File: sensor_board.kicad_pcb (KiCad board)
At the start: 2 copper layers, 28 parts, among them J1 DB9, P1 CONN_2, P2 CONN_2, P3 TORCH_ON, P4 ARC_OK, P5 TEST_POINTS, Q1 MOSFET_N, Q2 RELAY

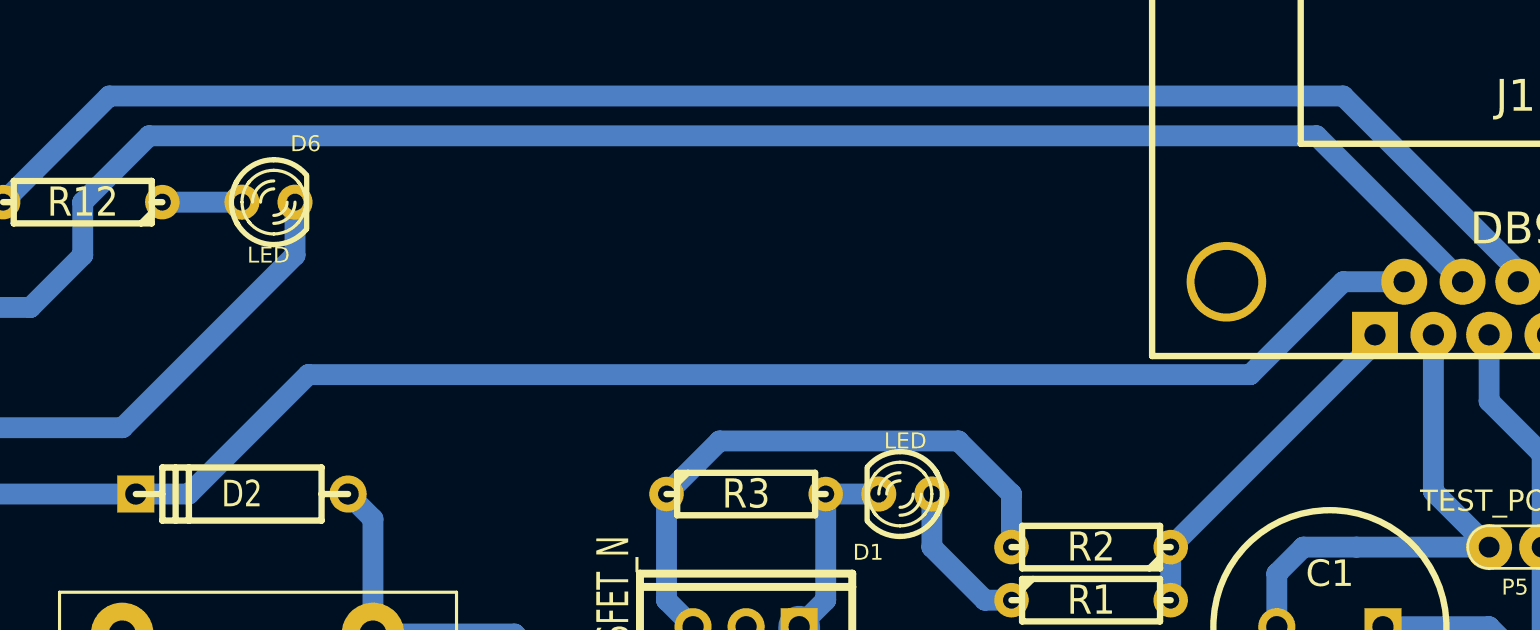
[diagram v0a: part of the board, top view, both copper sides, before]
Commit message: Fixed sensor board schematics- it's not wise to power relay from regulator
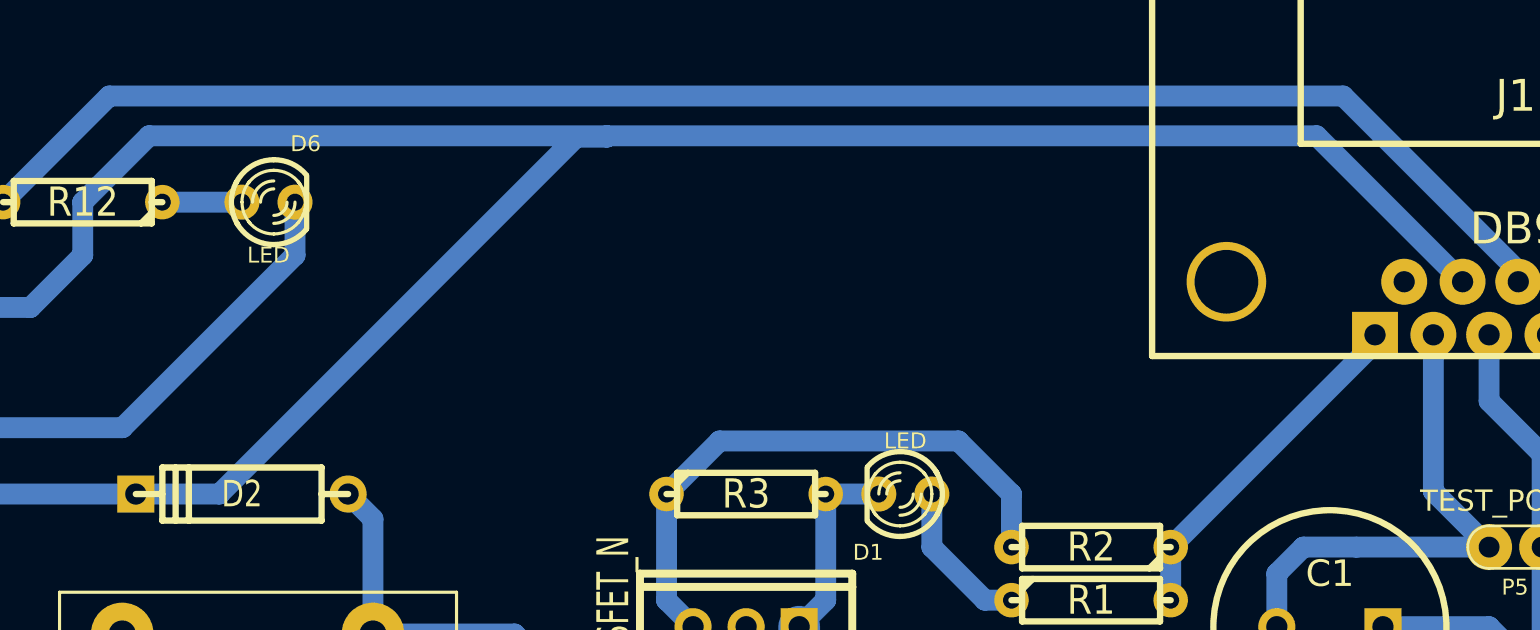
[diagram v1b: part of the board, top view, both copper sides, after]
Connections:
- D2 pad 2: +5V -> +12V
- J1 pad 6: +5V -> (no net)
- Q2 pad 1: +5V -> +12V
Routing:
- net +5V: track 133.3 -> 0.00 mm
- net +12V: track 87.5 -> 185.6 mm

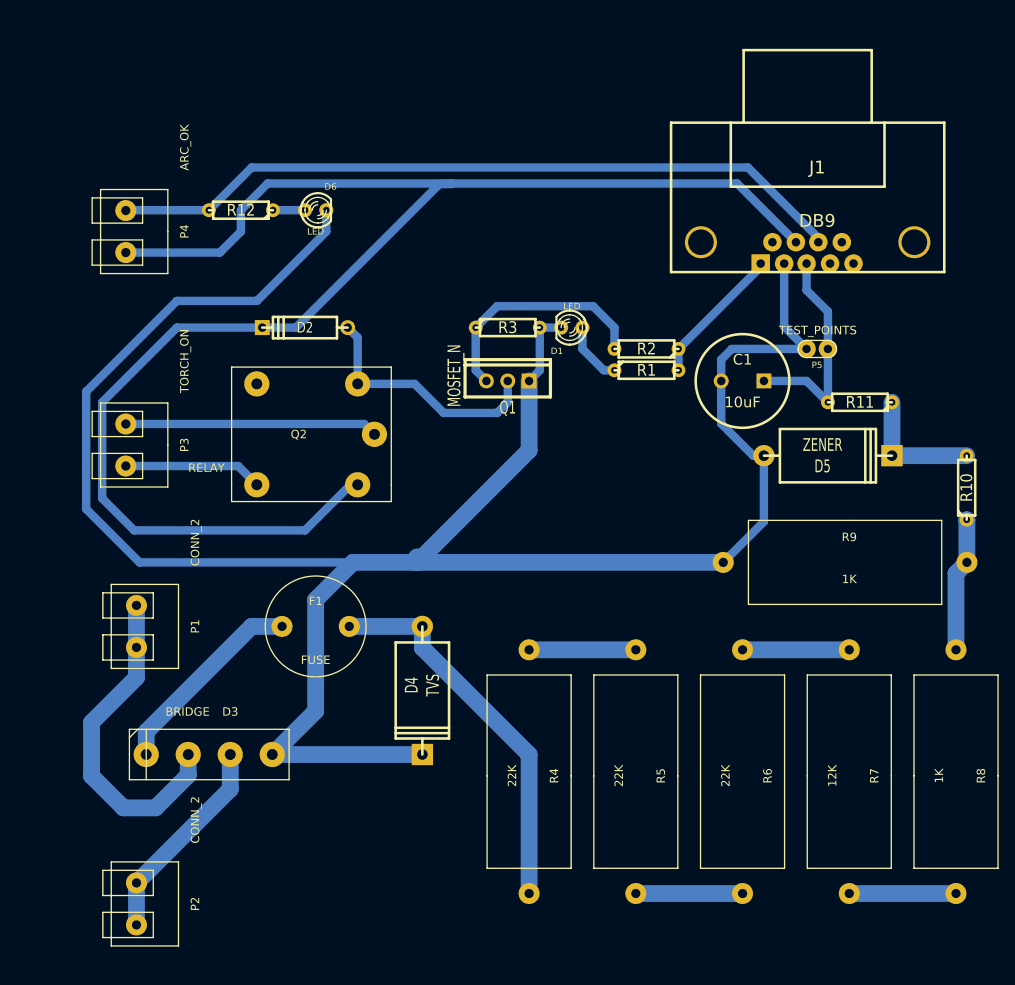
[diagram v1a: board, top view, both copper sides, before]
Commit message: Finished sensor board, started layout of controller board
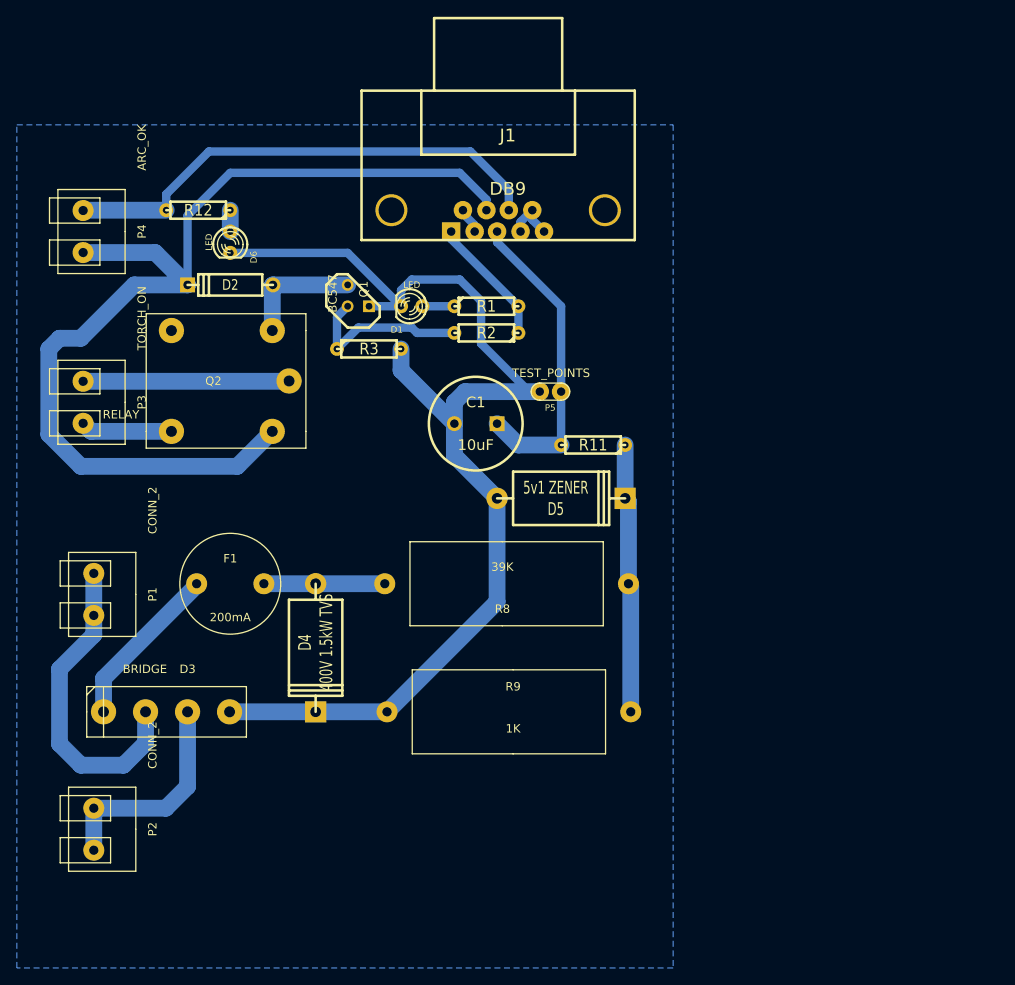
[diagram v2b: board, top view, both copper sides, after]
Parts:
- removed R10: 2R, R3-LARGE_PADS
- removed R4, R5, R6: 22K, R_5W_AXIAL
- removed R7: 12K, R_5W_AXIAL
- D4: value TVS -> 400V 1.5kW TVS
- D5: value ZENER -> 5v1 ZENER
- F1: value FUSE -> 200mA
- Q1: value MOSFET_N -> BC547; footprint TO220_VERT -> TO92-CBE
- R1: value 1K -> 3K3
- R8: value 1K -> 39K
- moved R8 58.6 mm to (85.7, 127.0), turned to 0 degrees
- moved R9 43.8 mm to (87.0, 142.2)
- moved J1 37.0 mm to (85.1, 83.8)
- moved R11 32.2 mm to (96.5, 110.5)
- moved C1 32.2 mm to (82.5, 108.0)
- moved D5 32.2 mm to (92.7, 116.8)
- moved P5 32.2 mm to (91.4, 104.1)
- moved R1 20.5 mm to (83.8, 94.0)
- moved Q1 20.5 mm to (68.6, 92.7)
- moved D1 19.2 mm to (74.9, 94.0)
- moved R2 19.1 mm to (83.8, 97.2)
- moved R3 16.7 mm to (69.8, 99.1)
- moved D4 13.7 mm to (63.5, 134.6)
- moved Q2 12.0 mm to (53.3, 102.9)
- moved F1 11.4 mm to (53.3, 127.0)
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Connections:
- D2 pad 1: N-000006 -> N-0000013
- D4 pad 1: N-0000018 -> N-0000011
- D5 pad 2: N-0000026 -> N-000009
- F1 pad 2: N-0000018 -> N-0000011
- J1 pad 4: (no net) -> GND
- J1 pad 5: (no net) -> GND
- J1 pad 6: (no net) -> GND
- J1 pad 9: (no net) -> GND
- Q2 pad 2: N-000006 -> N-0000013
- R11 pad 1: N-0000026 -> N-000009
- R2 pad 2: N-000007 -> N-0000012
- R3 pad 1: N-000007 -> N-0000012
- R8 pad 1: N-0000016 (its old number) -> N-0000011
- R8 pad 2: N-0000024 -> N-000009
- R9 pad 1: N-0000024 -> N-000009
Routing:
- net GND: track 264.8 -> 148.9 mm
- net +12V: track 185.6 -> 122.2 mm
- net N-0000018: track 45.7 -> 0.00 mm
- net N-000009: track 0.00 -> 32.0 mm
- net N-000006: track 29.6 -> 0.00 mm
- net /ARC_OK: track 88.5 -> 59.0 mm
- net N-000007: track 28.0 -> 0.00 mm
- net N-0000012: track 0.00 -> 20.9 mm
- net N-0000024: track 16.0 -> 0.00 mm
- net N-0000026: track 15.2 -> 0.00 mm
- net N-0000011: track 0.00 -> 14.4 mm
- net N-0000015 (its old number): track 12.7 -> 0.00 mm
- net N-0000014: track 12.7 -> 0.00 mm
- net N-0000016 (its old number): track 12.7 -> 0.00 mm
- net /FILT_SIG: track 26.2 -> 37.2 mm
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- added copper zone on B.Cu, net GND
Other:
- net class Other removed
- net class Wide removed
